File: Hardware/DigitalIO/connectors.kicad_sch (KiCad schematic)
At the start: 6 parts, among them J1 Conn_02x23_Odd_Even, J2 DIGITAL INPUT, J2 DIGITAL OUTPUT, J3 Conn_02x23_Odd_Even

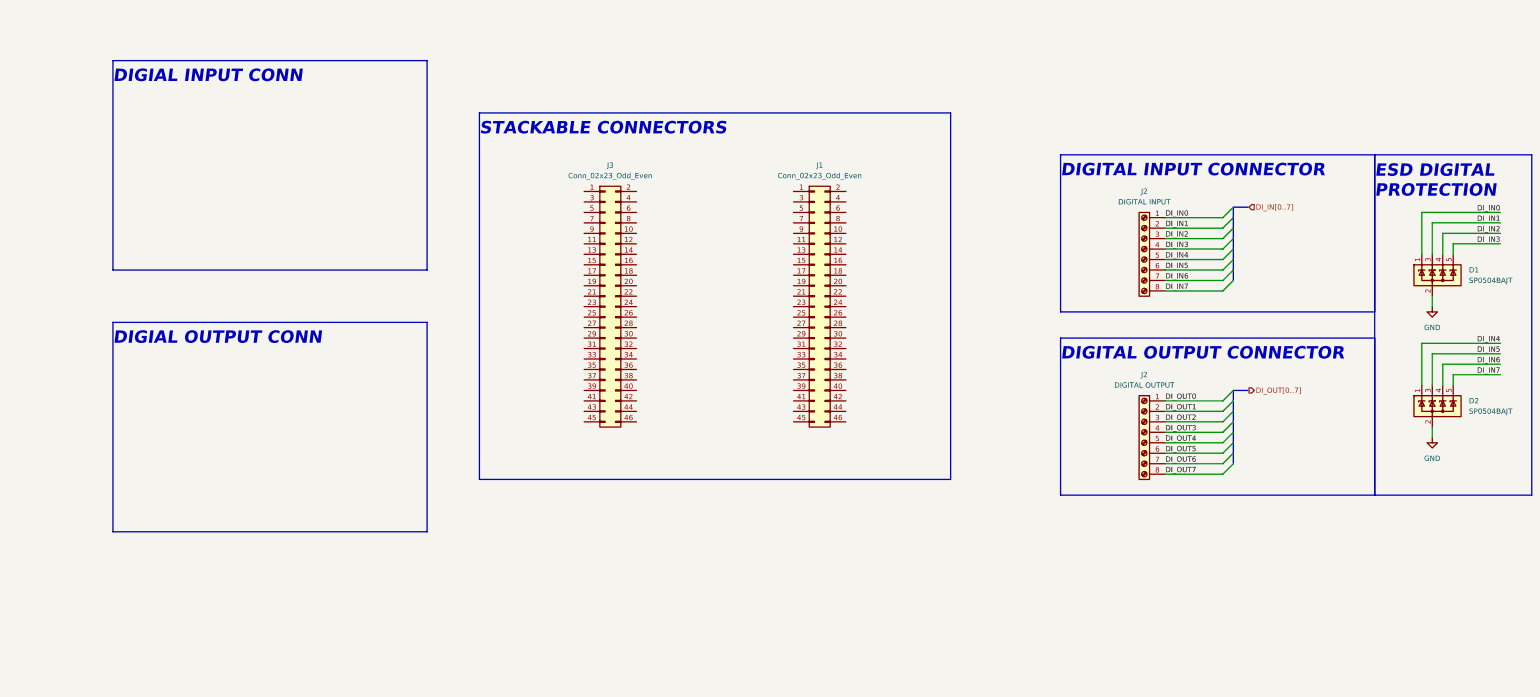
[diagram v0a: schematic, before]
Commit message: schematic update - all pcbs
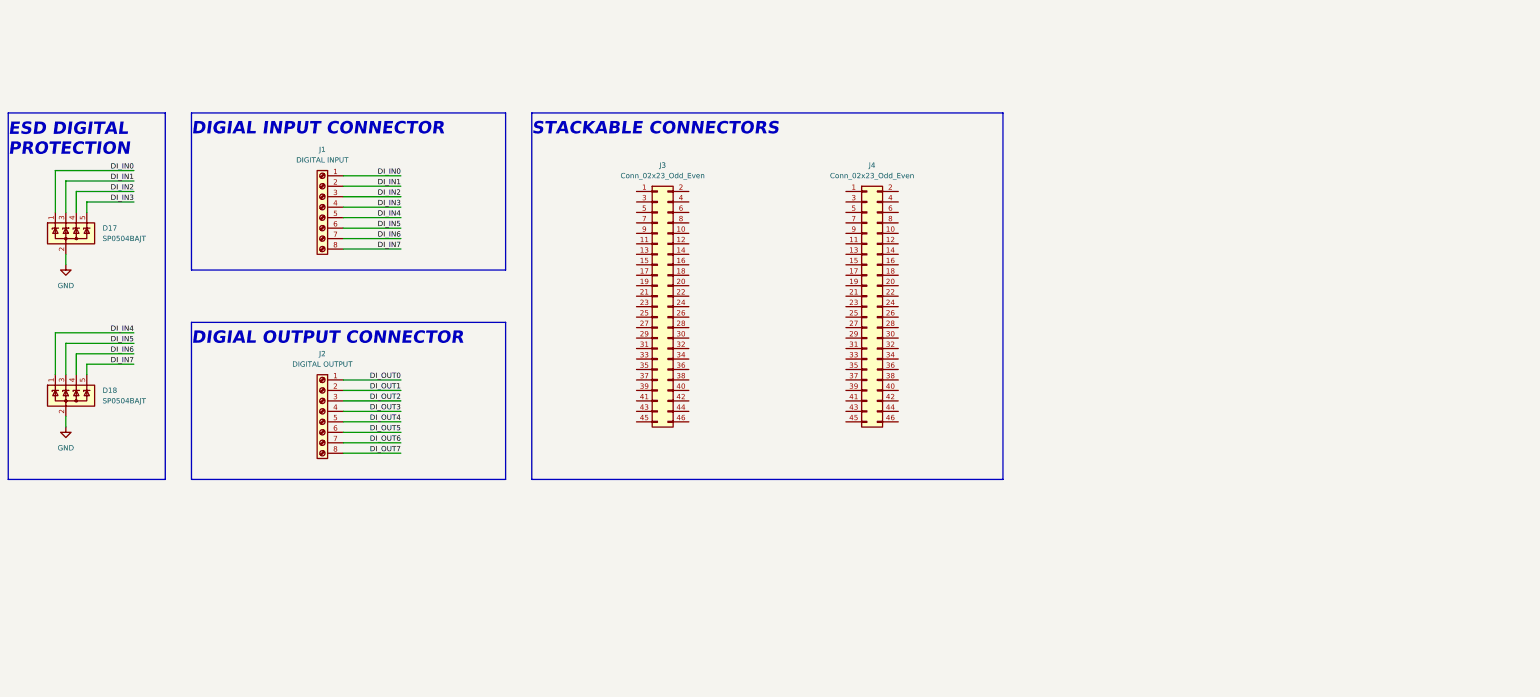
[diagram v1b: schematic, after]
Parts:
- removed J2: DIGITAL INPUT, symbol Connector:Screw_Terminal_01x08
- added J1: DIGITAL INPUT, symbol Connector:Screw_Terminal_01x08
- renumbered D1 to D17, D2 to D18, J1 to J4
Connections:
- net DI_IN0: now also J1.1 (Pin_1)
- net DI_IN1: now also J1.2 (Pin_2)
- net DI_IN2: now also J1.3 (Pin_3)
- net DI_IN3: now also J1.4 (Pin_4)
- net DI_IN4: now also J1.5 (Pin_5)
- net DI_IN5: now also J1.6 (Pin_6)
- net DI_IN6: now also J1.7 (Pin_7)
- net DI_IN7: now also J1.8 (Pin_8)
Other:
- note added: "DIGIAL INPUT CONNECTOR"
- note added: "DIGIAL OUTPUT CONNECTOR"
- note removed: "DIGIAL INPUT CONN"
- note removed: "DIGIAL OUTPUT CONN"
- note removed: "DIGITAL INPUT CONNECTOR"
- note removed: "DIGITAL OUTPUT CONNECTOR"
- moved on the sheet: D17, D18, J2, J3, J4

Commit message: schematic update - digital and analog footprints added
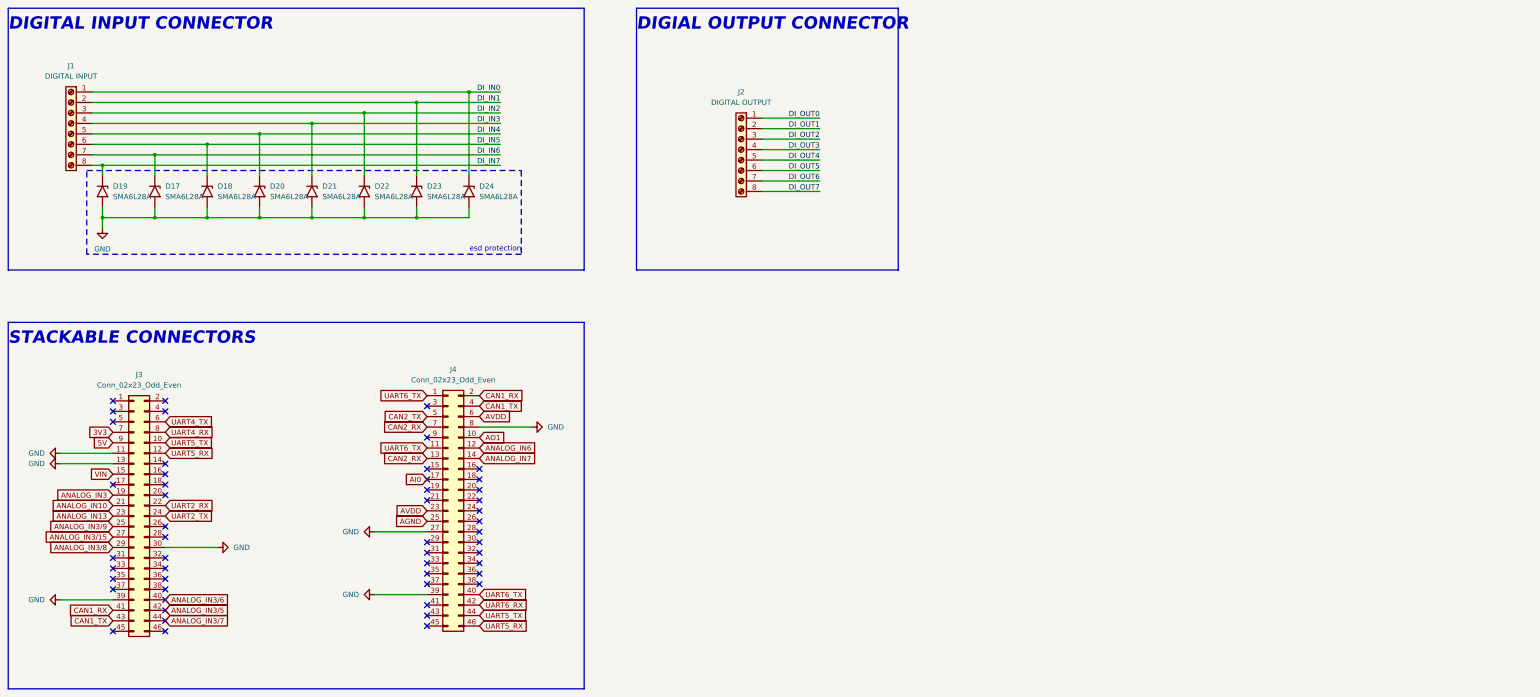
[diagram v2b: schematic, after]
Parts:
- removed D17, D18: SP0504BAJT, Package_TO_SOT_SMD:SOT-353_SC-70-5, symbol Power_Protection:SP0504BAJT
- added D17, D18, D19, D20, D21, D22, D23, D24: SMA6L28A, Diode_SMD:D_SMA, symbol Diode:SMAJ28A
- J1, J2: footprint (none) -> PLC_STM:1725711; Mouser Part Number (none) -> 651-1725711; Mouser Price/Stock (none) -> https://www.mouser.pl/ProductDetail/Phoenix-Contact/1725711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
- J3, J4: footprint PLC_STM_Power:PRT12790 -> PLC_STM:PRT12790
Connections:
- net DI_IN0: now also D24.1 (A1)
- net DI_IN1: now also D23.1 (A1)
- net DI_IN2: now also D22.1 (A1)
- net DI_IN3: now also D21.1 (A1)
- net DI_IN4: now also D20.1 (A1)
- net DI_IN5: now also D18.1 (A1)
- net DI_IN6: now also D17.1 (A1)
- net DI_IN7: now also D19.1 (A1)
- net GND: now also J3.11 (Pin_11), J3.13 (Pin_13), J3.30 (Pin_30), J3.39 (Pin_39), J4.27 (Pin_27), J4.39 (Pin_39), J4.8 (Pin_8), D17.2 (A2), D18.2 (A2), D19.2 (A2), D20.2 (A2), D21.2 (A2), D22.2 (A2), D23.2 (A2), D24.2 (A2)
- net UART6_TX: now reaches J4.1 (Pin_1)
- net UART6_TX: now also J4.11 (Pin_11), J4.40 (Pin_40)
- net AO1: now reaches J4.10 (Pin_10)
- net ANALOG_IN6: now reaches J4.12 (Pin_12)
- net CAN2_RX: now reaches J4.13 (Pin_13)
- net CAN2_RX: now also J4.7 (Pin_7)
- net ANALOG_IN7: now reaches J4.14 (Pin_14)
- net AI0: now reaches J4.17 (Pin_17)
- net CAN1_RX: now reaches J4.2 (Pin_2)
- net CAN1_RX: now also J3.41 (Pin_41)
- net AVDD: now reaches J4.23 (Pin_23)
- net AVDD: now also J4.6 (Pin_6)
- net AGND: now reaches J4.25 (Pin_25)
- net CAN1_TX: now reaches J4.4 (Pin_4)
- net CAN1_TX: now also J3.43 (Pin_43)
- net UART6_RX: now reaches J4.42 (Pin_42)
- net UART5_TX: now reaches J4.44 (Pin_44)
- net UART5_TX: now also J3.10 (Pin_10)
- net UART5_RX: now reaches J4.46 (Pin_46)
- net UART5_RX: now also J3.12 (Pin_12)
- net CAN2_TX: now reaches J4.5 (Pin_5)
- net VIN: now reaches J3.15 (Pin_15)
- net ANALOG_IN3: now reaches J3.19 (Pin_19)
- net ANALOG_IN10: now reaches J3.21 (Pin_21)
- net UART2_RX: now reaches J3.22 (Pin_22)
- net ANALOG_IN13: now reaches J3.23 (Pin_23)
- net UART2_TX: now reaches J3.24 (Pin_24)
- net ANALOG_IN3/9: now reaches J3.25 (Pin_25)
- net ANALOG_IN3/15: now reaches J3.27 (Pin_27)
- net ANALOG_IN3/8: now reaches J3.29 (Pin_29)
- net ANALOG_IN3/6: now reaches J3.40 (Pin_40)
- net ANALOG_IN3/5: now reaches J3.42 (Pin_42)
- net ANALOG_IN3/7: now reaches J3.44 (Pin_44)
- net UART4_TX: now reaches J3.6 (Pin_6)
- net 3V3: now reaches J3.7 (Pin_7)
- net UART4_RX: now reaches J3.8 (Pin_8)
- net 5V: now reaches J3.9 (Pin_9)
- no-connect marks 0 -> 51
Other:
- note added: "DIGITAL INPUT CONNECTOR"
- note added: "esd protection"
- note removed: "DIGIAL INPUT CONNECTOR"
- note removed: "ESD DIGITAL PROTECTION"
- moved on the sheet: J1, J2
